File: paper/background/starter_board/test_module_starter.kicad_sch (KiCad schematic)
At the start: 14 parts, among them J1 Barrel_Jack_12V, M1 ERM_Motor, M2 Stepper_4wire, M3 Servo_3pin, U1 D24V22F5_Buck, U2 Pi_Pico_W, U3 DRV2605L_Breakout, U4 DRV8871_Breakout, U5 Tic_T500

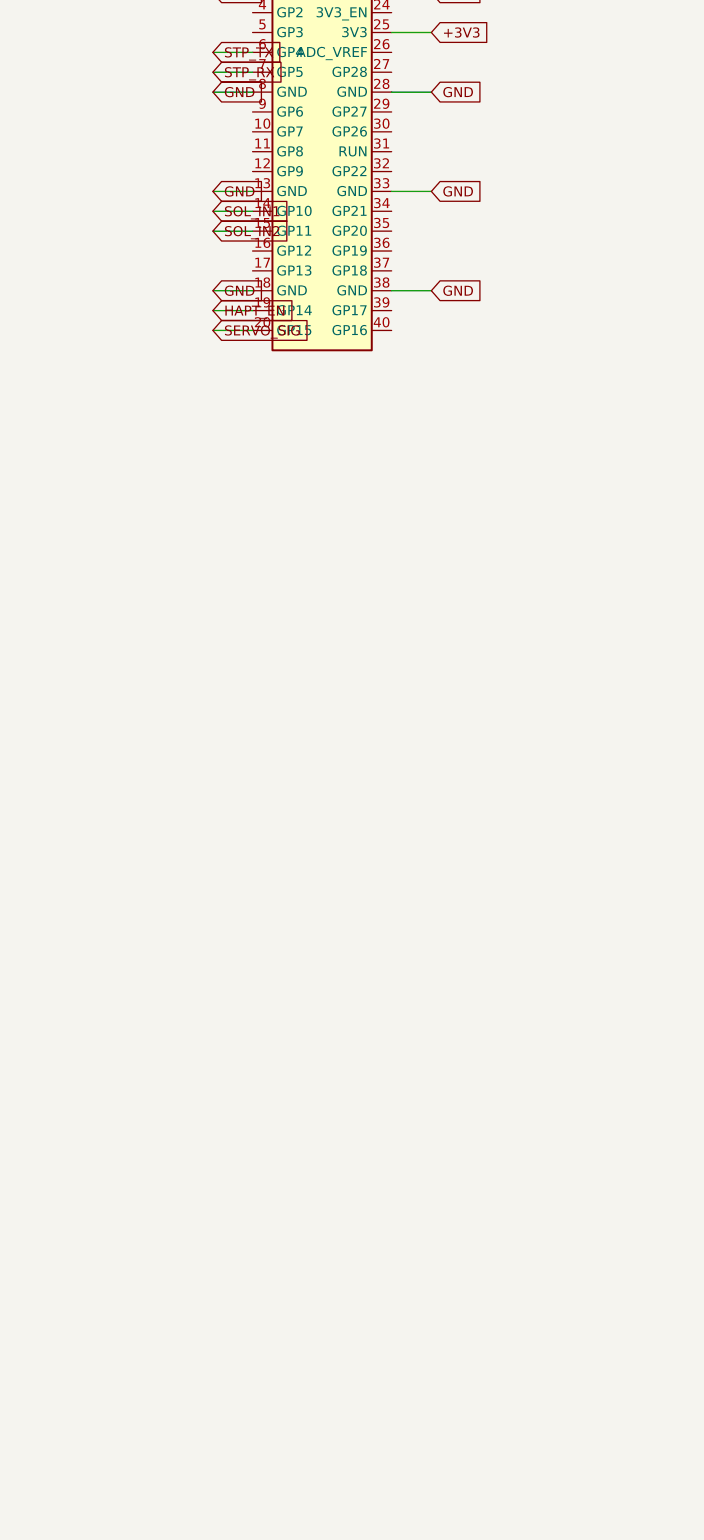
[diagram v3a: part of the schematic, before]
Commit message: Add Waveshare Pico-2CH-RS232 module footprint for scale integration
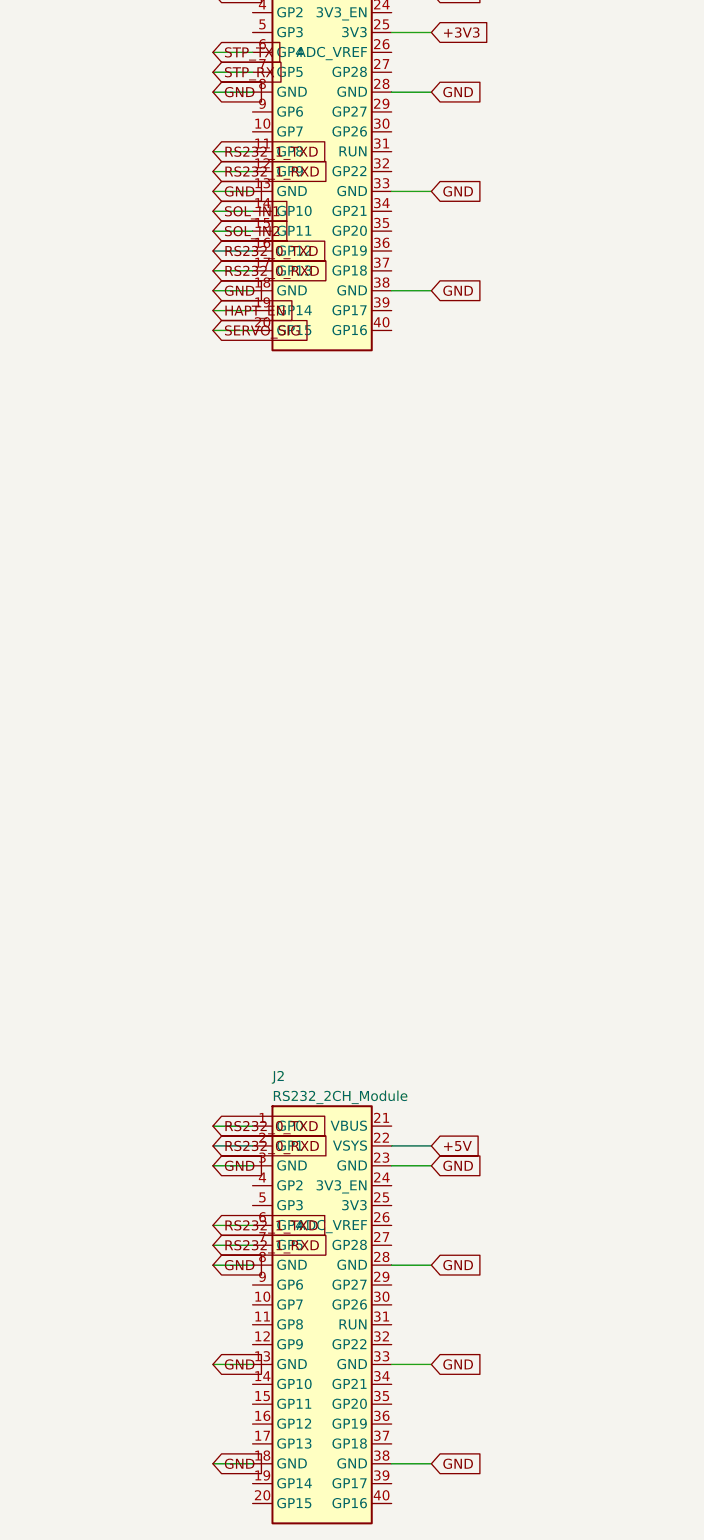
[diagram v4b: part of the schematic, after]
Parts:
- added J2: RS232_2CH_Module, powder_doser_parts:RS232_2CH_Module, symbol powder_doser_parts:RS232_2CH_Module
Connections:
- net +5V: now also J2.22 (VSYS)
- net GND: now also J2.13 (GND), J2.18 (GND), J2.23 (GND), J2.28 (GND), J2.3 (GND), J2.33 (GND), J2.38 (GND), J2.8 (GND)
- net RS232_1_TXD: now reaches U2.11 (GP8)
- net RS232_1_TXD: now also J2.6 (GP4)
- net RS232_1_RXD: now reaches U2.12 (GP9)
- net RS232_1_RXD: now also J2.7 (GP5)
- net RS232_0_TXD: now reaches U2.16 (GP12)
- net RS232_0_TXD: now also J2.1 (GP0)
- net RS232_0_RXD: now reaches U2.17 (GP13)
- net RS232_0_RXD: now also J2.2 (GP1)
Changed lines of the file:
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@@
+    (effects (font (size 1.27 1.27)) (justify left))
+  )
+  (wire (pts (xy 101.11 51.27) (xy 96.03 51.27))
+    (stroke (width 0) (type default))
+  )
+  (global_label "RS232_1_TXD" (shape input) (at 96.03 51.27 180) (fields_autoplaced)
+    (effects (font (size 1.27 1.27)) (justify left))
+  )
+  (wire (pts (xy 101.11 53.81) (xy 96.03 53.81))
+    (stroke (width 0) (type default))
+  )
+  (global_label "RS232_1_RXD" (shape input) (at 96.03 53.81 180) (fields_autoplaced)
     (effects (font (size 1.27 1.27)) (justify left))
   )
@@
     (effects (font (size 1.27 1.27)) (justify left))
   )
+  (wire (pts (xy 101.11 63.97) (xy 96.03 63.97))
+    (stroke (width 0) (type default))
+  )
+  (global_label "RS232_0_TXD" (shape input) (at 96.03 63.97 180) (fields_autoplaced)
+    (effects (font (size 1.27 1.27)) (justify left))
+  )
+  (wire (pts (xy 101.11 66.51) (xy 96.03 66.51))
+    (stroke (width 0) (type default))
+  )
+  (global_label "RS232_0_RXD" (shape input) (at 96.03 66.51 180) (fields_autoplaced)
+    (effects (font (size 1.27 1.27)) (justify left))
+  )
   (wire (pts (xy 101.11 69.05) (xy 96.03 69.05))
     (stroke (width 0) (type default))
@@
     (effects (font (size 1.27 1.27)) (justify left))
   )
+  (symbol (lib_id "powder_doser_parts:RS232_2CH_Module") (at 110 200 0) (unit 1)
+    (in_bom yes) (on_board yes) (dnp no)
+    (property "Reference" "J2" (id 0) (at 103.65 169.52 0)
+      (effects (font (size 1.27 1.27)) (justify left)))
+    (property "Value" "RS232_2CH_Module" (id 1) (at 103.65 172.06 0)
+      (effects (font (size 1.27 1.27)) (justify left)))
+    (property "Footprint" "powder_doser_parts:RS232_2CH_Module" (id 2) (at 110 200 0)
+      (effects (font (size 1.27 1.27)) hide))
+    (property "Datasheet" "" (id 3) (at 110 200 0)
+      (effects (font (size 1.27 1.27)) hide))
+    (instances
+      (project "test_module_starter"
+        (path "/00000000-0000-0000-0003-000000000001" (reference "J2") (unit 1))
+      )
+    )
+  )
+  (wire (pts (xy 101.11 175.87) (xy 96.03 175.87))
+    (stroke (width 0) (type default))
+  )
+  (global_label "RS232_0_TXD" (shape input) (at 96.03 175.87 180) (fields_autoplaced)
+    (effects (font (size 1.27 1.27)) (justify left))
+  )
+  (wire (pts (xy 101.11 178.41) (xy 96.03 178.41))
+    (stroke (width 0) (type default))
+  )
+  (global_label "RS232_0_RXD" (shape input) (at 96.03 178.41 180) (fields_autoplaced)
+    (effects (font (size 1.27 1.27)) (justify left))
+  )
+  (wire (pts (xy 101.11 180.95) (xy 96.03 180.95))
+    (stroke (width 0) (type default))
+  )
+  (global_label "GND" (shape input) (at 96.03 180.95 180) (fields_autoplaced)
+    (effects (font (size 1.27 1.27)) (justify left))
+  )
+  (wire (pts (xy 101.11 188.57) (xy 96.03 188.57))
+    (stroke (width 0) (type default))
+  )
+  (global_label "RS232_1_TXD" (shape input) (at 96.03 188.57 180) (fields_autoplaced)
+    (effects (font (size 1.27 1.27)) (justify left))
+  )
+  (wire (pts (xy 101.11 191.11) (xy 96.03 191.11))
+    (stroke (width 0) (type default))
+  )
+  (global_label "RS232_1_RXD" (shape input) (at 96.03 191.11 180) (fields_autoplaced)
+    (effects (font (size 1.27 1.27)) (justify left))
+  )
+  (wire (pts (xy 101.11 193.65) (xy 96.03 193.65))
+    (stroke (width 0) (type default))
+  )
+  (global_label "GND" (shape input) (at 96.03 193.65 180) (fields_autoplaced)
+    (effects (font (size 1.27 1.27)) (justify left))
+  )
+  (wire (pts (xy 101.11 206.35) (xy 96.03 206.35))
+    (stroke (width 0) (type default))
+  )
+  (global_label "GND" (shape input) (at 96.03 206.35 180) (fields_autoplaced)
+    (effects (font (size 1.27 1.27)) (justify left))
+  )
+  (wire (pts (xy 101.11 219.05) (xy 96.03 219.05))
+    (stroke (width 0) (type default))
+  )
+  (global_label "GND" (shape input) (at 96.03 219.05 180) (fields_autoplaced)
+    (effects (font (size 1.27 1.27)) (justify left))
+  )
+  (wire (pts (xy 118.89 178.41) (xy 123.97 178.41))
+    (stroke (width 0) (type default))
+  )
+  (global_label "+5V" (shape input) (at 123.97 178.41 0) (fields_autoplaced)
+    (effects (font (size 1.27 1.27)) (justify left))
+  )
+  (wire (pts (xy 118.89 180.95) (xy 123.97 180.95))
+    (stroke (width 0) (type default))
+  )
+  (global_label "GND" (shape input) (at 123.97 180.95 0) (fields_autoplaced)
+    (effects (font (size 1.27 1.27)) (justify left))
+  )
+  (wire (pts (xy 118.89 193.65) (xy 123.97 193.65))
+    (stroke (width 0) (type default))
+  )
+  (global_label "GND" (shape input) (at 123.97 193.65 0) (fields_autoplaced)
+    (effects (font (size 1.27 1.27)) (justify left))
+  )
+  (wire (pts (xy 118.89 206.35) (xy 123.97 206.35))
+    (stroke (width 0) (type default))
+  )
+  (global_label "GND" (shape input) (at 123.97 206.35 0) (fields_autoplaced)
+    (effects (font (size 1.27 1.27)) (justify left))
+  )
+  (wire (pts (xy 118.89 219.05) (xy 123.97 219.05))
+    (stroke (width 0) (type default))
+  )
+  (global_label "GND" (shape input) (at 123.97 219.05 0) (fields_autoplaced)
+    (effects (font (size 1.27 1.27)) (justify left))
+  )
